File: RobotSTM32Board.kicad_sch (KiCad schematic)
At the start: 19 parts, among them IC1 TB6612FNG, IC2 TB6612FNG, J1 MotorA, J2 MotorB, J3 MotorC, J4 MotorD, J5 EncoderA, J6 EncoderB, J7 EncoderC, J8 EncoderD, J9 ESTOP, U1 NUCLEO-F410RB, U2 BNO085, U3 ESP32-S3-WROOM-1

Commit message: did motor driver and sttuff
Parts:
- removed U3: ESP32-S3-WROOM-1, RF_Module:ESP32-S3-WROOM-1, symbol RF_Module:ESP32-S3-WROOM-1
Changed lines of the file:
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@@
-	)
-	(symbol
-		(lib_id "RF_Module:ESP32-S3-WROOM-1")
-		(at -50.8 115.57 0)
-		(unit 1)
-		(exclude_from_sim no)
-		(in_bom yes)
-		(on_board yes)
-		(dnp no)
-		(fields_autoplaced yes)
-		(property "Reference" "U3"
-			(at -48.6059 85.09 0)
-			(effects
-				(font
-					(size 1.27 1.27)
-				)
-				(justify left)
-			)
-		)
-		(property "Value" "ESP32-S3-WROOM-1"
-			(at -48.6059 87.63 0)
-			(effects
-				(font
-					(size 1.27 1.27)
-				)
-				(justify left)
-			)
-		)
-		(property "Footprint" "RF_Module:ESP32-S3-WROOM-1"
-			(at -50.8 113.03 0)
-			(effects
-				(font
-					(size 1.27 1.27)
-				)
-				(hide yes)
-			)
-		)
-		(property "Datasheet" "https://www.espressif.com/sites/default/files/documentation/esp32-s3-wroom-1_wroom-1u_datasheet_en.pdf"
-			(at -50.8 115.57 0)
-			(effects
-				(font
-					(size 1.27 1.27)
-				)
-				(hide yes)
-			)
-		)
-		(property "Description" "RF Module, ESP32-S3 SoC, Wi-Fi 802.11b/g/n, Bluetooth, BLE, 32-bit, 3.3V, onboard antenna, SMD"
-			(at -50.8 115.57 0)
-			(effects
-				(font
-					(size 1.27 1.27)
-				)
-				(hide yes)
-			)
-		)
-		(pin "41"
-		)
-		(pin "34"
-		)
-		(pin "33"
-		)
-		(pin "38"
-		)
-		(pin "29"
-		)
-		(pin "23"
-		)
-		(pin "22"
-		)
-		(pin "27"
-		)
-		(pin "10"
-		)
-		(pin "14"
-		)
-		(pin "6"
-		)
-		(pin "20"
-		)
-		(pin "35"
-		)
-		(pin "17"
-		)
-		(pin "28"
-		)
-		(pin "25"
-		)
-		(pin "19"
-		)
-		(pin "13"
-		)
-		(pin "24"
-		)
-		(pin "12"
-		)
-		(pin "11"
-		)
-		(pin "26"
-		)
-		(pin "8"
-		)
-		(pin "7"
-		)
-		(pin "1"
-		)
-		(pin "5"
-		)
-		(pin "32"
-		)
-		(pin "39"
-		)
-		(pin "30"
-		)
-		(pin "21"
-		)
-		(pin "18"
-		)
-		(pin "31"
-		)
-		(pin "36"
-		)
-		(pin "37"
-		)
-		(pin "9"
-		)
-		(pin "40"
-		)
-		(pin "15"
-		)
-		(pin "3"
-		)
-		(pin "4"
-		)
-		(pin "16"
-		)
-		(pin "2"
-		)
-		(instances
-			(project ""
-				(path "/ac0c4a11-3af6-428a-b627-4ab879a3dd88"
-					(reference "U3")
-					(unit 1)
-				)
-			)
-		)
 	)
 	(symbol

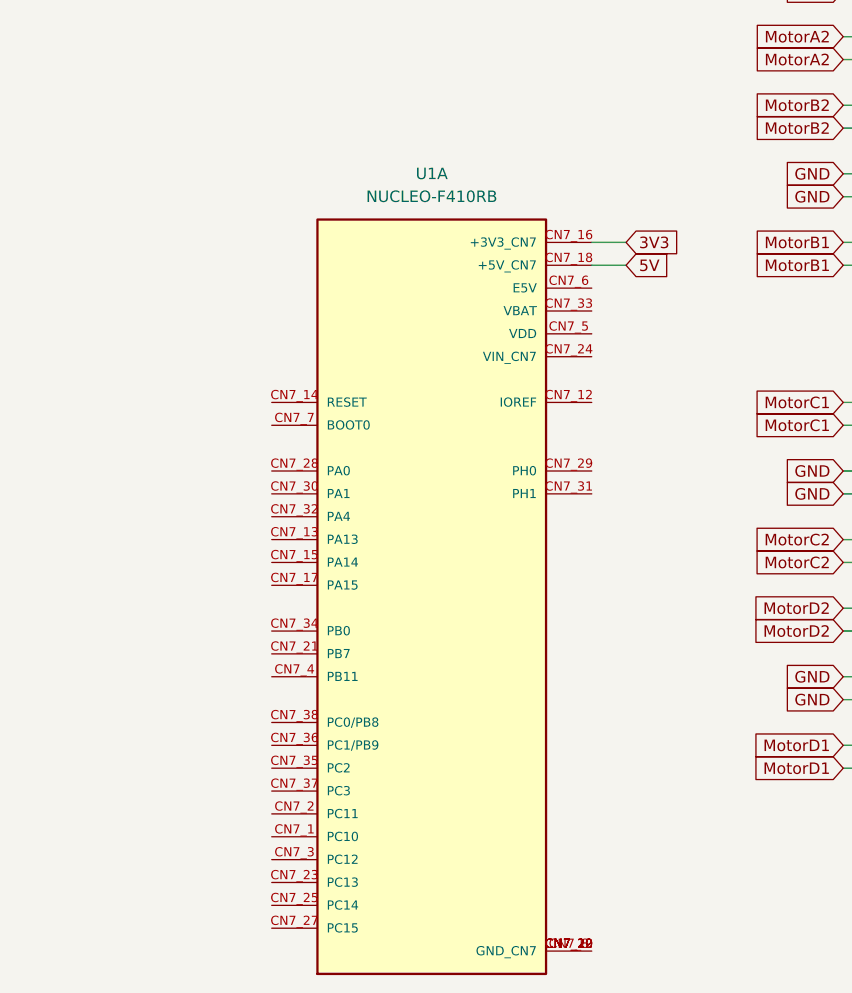
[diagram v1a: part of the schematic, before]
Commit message: changed board to the one peter wilson gave us
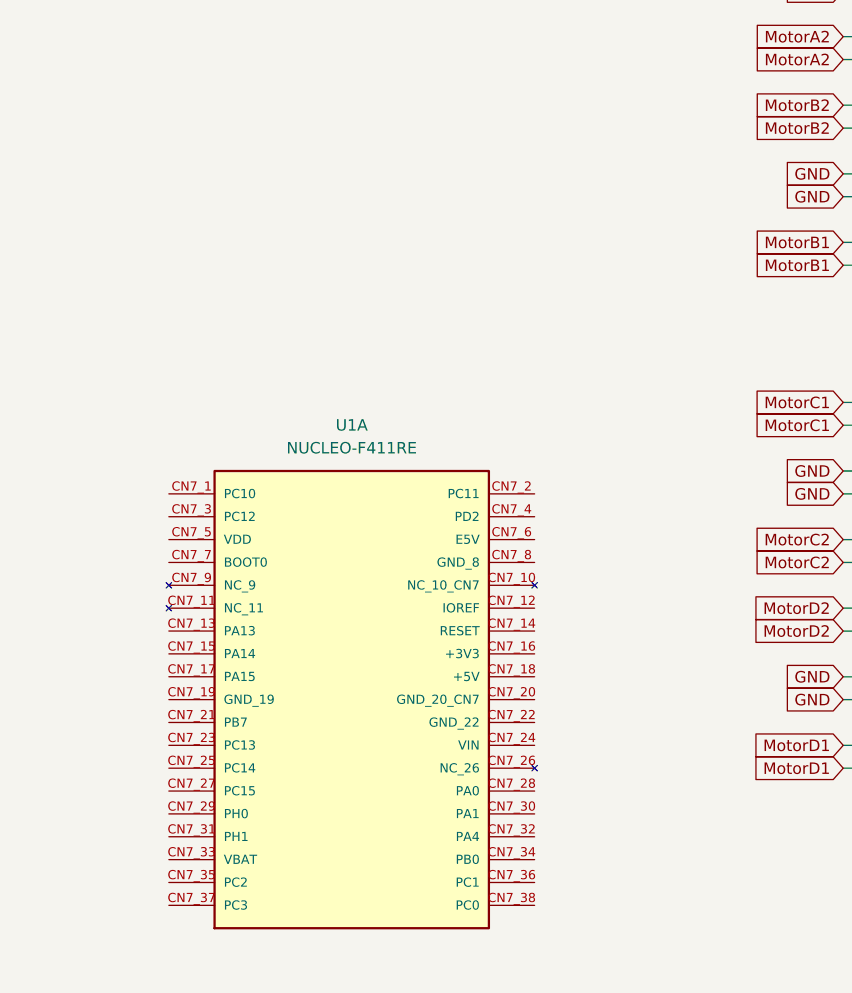
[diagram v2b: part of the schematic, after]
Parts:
- removed U1: NUCLEO-F410RB, NUCLEO-F410RB:ST_NUCLEO-F410RB, symbol NUCLEO-F410RB:NUCLEO-F410RB
- added U1: NUCLEO-F411RE, NUCLEO-F411RE:BOARD_NUCLEO-F411RE, symbol NUCLEO-F411RE:NUCLEO-F411RE

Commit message: added buck converter 6v to schematic
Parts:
- added C10, C13, C22: 10uF, symbol Device:C_Small
- added C11, C7: 1uF, symbol Device:C_Small
- added C12, C20: 220nF, symbol Device:C_Small
- added C14: 27nf, symbol Device:C_Small
- added C15: 100nF, symbol Device:C_Small
- added C16, C18: 1.2nF, symbol Device:C_Small
- added C17: 180pF, symbol Device:C_Small
- added C19, C4, C5, C9: C_Small, symbol Device:C_Small
- added C21: 120pF, symbol Device:C_Small
- added C6: NC, symbol Device:C_Small
- added C8: 0.1uF, symbol Device:C_Small
- added D1: D_Zener_Small_Filled, symbol Device:D_Zener_Small_Filled
- added L1: L_Small, symbol Device:L_Small
- added L2: 1.5uH, symbol Device:L_Small
- added L3: 1uH, symbol Device:L_Small
- added Q1: NPN, symbol Simulation_SPICE:NPN
- added Q2, Q3: NMOS_Substrate, symbol Simulation_SPICE:NMOS_Substrate
- added R10: 56.2k, symbol Device:R_Small
- added R11: 11k, symbol Device:R_Small
- added R12: 86.6k, symbol Device:R_Small
- added R13: 2.55k, symbol Device:R_Small
- added R14: 7.5k, symbol Device:R_Small
- added R15: 2.5k, symbol Device:R_Small
- added R16: 976, symbol Device:R_Small
- added R17, R7: 20k, symbol Device:R_Small
- added R18: 2.23k, symbol Device:R_Small
- added R19: 225, symbol Device:R_Small
- added R3, R4, R5: R_Small, symbol Device:R_Small
- added R6: 130k, symbol Device:R_Small
- added R8: 100k, symbol Device:R_Small
- added R9: 2.21, symbol Device:R_Small
- added U3: TPS564252DRLR, TPS564252DRLR:SOT50P160X60-6N, symbol TPS564252DRLR:TPS564252DRLR
- added U4: TPS51386RJNR, TPS51386RJNR:VREG_TPS51386RJNR, symbol TPS51386RJNR:TPS51386RJNR
- added U5: LM27403SQ/NOPB, RTW24, symbol 2025-03-13_17-27-54:LM27403SQ_NOPB
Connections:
- net +3V3: now also C5.1, L1.2, R3.1
- net +5V: now also C9.1, L2.2, R6.1
- net +6V: now also C20.2, C21.2, C22.2, L3.2, R14.2, R17.2
- net GND: now also C10.2, C11.2, C13.2, C14.2, C15.2, C16.2, C22.1, C4.2, C5.2, C6.2, C7.2, C9.2, Q1.3 (E), Q3.3 (S), Q3.4 (Bulk), R11.2, R12.2, R18.1, R4.2, R7.2, R8.2, U3.3 (GND), U4.10 (AGND), U4.12 (MODE), U4.2 (PGND), U5.10 (D-), U5.13 (GND), U5.2 (RS)
- new net: R6.2, R7.1, U4.4 (FB)
- new net: C16.1, Q1.1 (C), Q1.2 (B), U5.9 (D+)
- new net: R10.1, U5.11 (PGOOD)
- new net: C13.1, D1.2 (A), R10.2, U5.14 (VDD)
- new net: C15.1, R12.1, U5.8 (OTP)
- new net: C12.1, D1.1 (K), U5.18 (CBOOT)
- new net: C12.2, L3.1, Q2.3 (S), Q2.4 (Bulk), Q3.1 (D), R16.2, U5.16 (SW)
- new net: C17.2, R13.2, R17.1, R18.2, R19.1, U5.3 (FB)
- new net: Q2.2 (G), U5.17 (HG)
- new net: C11.1, R9.1, U5.12 (VIN)
- new net: C17.1, C18.1, U5.4 (COMP)
- new net: R11.1, U5.5 (FADJ)
- new net: R8.1, U4.3 (PG)
- new net: C18.2, R13.1
- new net: C6.1, U4.5 (SS)
- new net: C8.2, L2.1, U4.7 (SW)
- new net: C8.1, U4.8 (VBST)
- new net: C20.1, R15.2, R16.1
- new net: C19.2, R14.1, U5.24 (CS-)
- new net: C19.1, R15.1, U5.23 (CS+)
- new net: R3.2, R4.1, U3.6 (FB)
- new net: C21.1, R19.2
- new net: L1.1, U3.2 (SW)
- new net: R5.1, U3.4 (PG)
- new net: C14.1, U5.1 (SS/TRACK)
- new net: Q3.2 (G), U5.15 (LG)
- new net Vin: C10.1, C4.1, C7.1, Q2.1 (D), R5.2, R9.2, U3.1 (VIN), U3.5 (EN), U4.1 (VIN), U4.11 (EN), U4.9 (VCC)

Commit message: pcb layout for the buck converters started
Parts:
- added J10: Qwiik1, Connector_JST:JST_SH_BM04B-SRSS-TB_1x04-1MP_P1.00mm_Vertical, symbol Connector:Conn_01x04_Socket
- added J11: Qwiik2, Connector_JST:JST_SH_BM04B-SRSS-TB_1x04-1MP_P1.00mm_Vertical, symbol Connector:Conn_01x04_Socket
- added J12: Qwiik3, Connector_JST:JST_SH_BM04B-SRSS-TB_1x04-1MP_P1.00mm_Vertical, symbol Connector:Conn_01x04_Socket
- added J13: Qwiik4, Connector_JST:JST_SH_BM04B-SRSS-TB_1x04-1MP_P1.00mm_Vertical, symbol Connector:Conn_01x04_Socket
- added J14: Qwiik5, Connector_JST:JST_SH_BM04B-SRSS-TB_1x04-1MP_P1.00mm_Vertical, symbol Connector:Conn_01x04_Socket
- C10, C11, C12, C13, C14, C15, C16, C17, C18, C19, C20, C21, C22, C4, C5, C6, C7, C8: footprint (none) -> Capacitor_SMD:C_0603_1608Metric
- C9: value C_Small -> 22uf; footprint (none) -> Capacitor_SMD:C_0603_1608Metric
- D1: footprint (none) -> Diode_SMD:D_0603_1608Metric
- L1, L2, L3: footprint (none) -> Inductor_SMD:L_0805_2012Metric
- Q1, Q2, Q3: footprint (none) -> Package_TO_SOT_SMD:SOT-23
- R10, R11, R12, R13, R14, R15, R16, R17, R18, R19, R3, R4, R5, R6, R7, R8, R9: footprint (none) -> Resistor_SMD:R_0603_1608Metric
- U5: footprint RTW24 -> footprints:RTW24
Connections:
- net GND: now also U5.25 (EPAD)
- net MotorACCW: now also U1.CN7_2 (PC11)
- net MotorACW: now also U1.CN7_3 (PC12)
- net MotorBCCW: now also U1.CN7_4 (PD2)
- net MotorBCW: now also U1.CN7_13 (PA13)
- net MotorPWMA: now also U1.CN7_1 (PC10)
